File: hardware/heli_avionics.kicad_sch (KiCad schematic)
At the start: 15 parts, among them J1 Pin_Header_2x3, J7 JST_ZH_01x02, SW1 Reset, U1 ATmega4808-A

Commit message: Added mounting holes and did board outline
Also tried an initial layout with some components
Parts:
- added H1, H2, H3: MountingHole, MountingHole:MountingHole_2mm, symbol Mechanical:MountingHole
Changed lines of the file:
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@@
+		)
+	)
+	(rectangle
+		(start 243.84 124.46)
+		(end 271.78 152.4)
+		(stroke
+			(width 0)
+			(type dash_dot_dot)
+		)
+		(fill
+			(type none)
 		)
 	)
@@
 	)
 	(symbol
+		(lib_id "Mechanical:MountingHole")
+		(at 250.19 146.05 0)
+		(unit 1)
+		(exclude_from_sim yes)
+		(in_bom no)
+		(on_board yes)
+		(dnp no)
+		(fields_autoplaced yes)
+		(property "Reference" "H3"
+			(at 252.73 144.7799 0)
+			(effects
+				(font
+					(size 1.27 1.27)
+				)
+				(justify left)
+			)
+		)
+		(property "Value" "MountingHole"
+			(at 252.73 147.3199 0)
+			(effects
+				(font
+					(size 1.27 1.27)
+				)
+				(justify left)
+			)
+		)
+		(property "Footprint" "MountingHole:MountingHole_2mm"
+			(at 250.19 146.05 0)
+			(effects
+				(font
+					(size 1.27 1.27)
+				)
+				(hide yes)
+			)
+		)
+		(property "Datasheet" "~"
+			(at 250.19 146.05 0)
+			(effects
+				(font
+					(size 1.27 1.27)
+				)
+				(hide yes)
+			)
+		)
+		(property "Description" "Mounting Hole without connection"
+			(at 250.19 146.05 0)
+			(effects
+				(font
+					(size 1.27 1.27)
+				)
+				(hide yes)
+			)
+		)
+		(instances
+			(project ""
+				(path "/c384ea46-0dfb-4673-b2f4-1f88fafbcaa5"
+					(reference "H3")
+					(unit 1)
+				)
+			)
+		)
+	)
+	(symbol
 		(lib_id "Device:C")
 		(at 60.96 68.58 0)
@@
 	)
 	(symbol
+		(lib_id "Mechanical:MountingHole")
+		(at 250.19 138.43 0)
+		(unit 1)
+		(exclude_from_sim yes)
+		(in_bom no)
+		(on_board yes)
+		(dnp no)
+		(fields_autoplaced yes)
+		(property "Reference" "H2"
+			(at 252.73 137.1599 0)
+			(effects
+				(font
+					(size 1.27 1.27)
+				)
+				(justify left)
+			)
+		)
+		(property "Value" "MountingHole"
+			(at 252.73 139.6999 0)
+			(effects
+				(font
+					(size 1.27 1.27)
+				)
+				(justify left)
+			)
+		)
+		(property "Footprint" "MountingHole:MountingHole_2mm"
+			(at 250.19 138.43 0)
+			(effects
+				(font
+					(size 1.27 1.27)
+				)
+				(hide yes)
+			)
+		)
+		(property "Datasheet" "~"
+			(at 250.19 138.43 0)
+			(effects
+				(font
+					(size 1.27 1.27)
+				)
+				(hide yes)
+			)
+		)
+		(property "Description" "Mounting Hole without connection"
+			(at 250.19 138.43 0)
+			(effects
+				(font
+					(size 1.27 1.27)
+				)
+				(hide yes)
+			)
+		)
+		(instances
+			(project ""
+				(path "/c384ea46-0dfb-4673-b2f4-1f88fafbcaa5"
+					(reference "H2")
+					(unit 1)
+				)
+			)
+		)
+	)
+	(symbol
 		(lib_id "power:GND")
 		(at 205.74 106.68 0)
@@
 					(unit 1)
 				)
+			)
+		)
+	)
+	(symbol
+		(lib_id "Mechanical:MountingHole")
+		(at 250.19 130.81 0)
+		(unit 1)
+		(exclude_from_sim yes)
+		(in_bom no)
+		(on_board yes)
+		(dnp no)
+		(fields_autoplaced yes)
+		(property "Reference" "H1"
+			(at 252.73 129.5399 0)
+			(effects
+				(font
+					(size 1.27 1.27)
+				)
+				(justify left)
+			)
+		)
+		(property "Value" "MountingHole"
+			(at 252.73 132.0799 0)
+			(effects
+				(font
+					(size 1.27 1.27)
+				)
+				(justify left)
+			)
+		)
+		(property "Footprint" "MountingHole:MountingHole_2mm"
+			(at 250.19 130.81 0)
+			(effects
+				(font
+					(size 1.27 1.27)
+				)
+				(hide yes)
+			)
+		)
+		(property "Datasheet" "~"
+			(at 250.19 130.81 0)
+			(effects
+				(font
+					(size 1.27 1.27)
+				)
+				(hide yes)
+			)
+		)
+		(property "Description" "Mounting Hole without connection"
+			(at 250.19 130.81 0)
+			(effects
+				(font
+					(size 1.27 1.27)
+				)
+				(hide yes)
+			)
+		)
+		(instances
+			(project ""
+				(path "/c384ea46-0dfb-4673-b2f4-1f88fafbcaa5"
+					(reference "H1")
+					(unit 1)
+				)

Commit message: Assigned footprints for capacitors and inductors
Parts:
- C1, C2, C28, C29, C3: footprint (none) -> Capacitor_SMD:C_0603_1608Metric_Pad1.08x0.95mm_HandSolder
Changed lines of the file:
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@@
 			)
 		)
-		(property "Footprint" ""
+		(property "Footprint" "Capacitor_SMD:C_0603_1608Metric_Pad1.08x0.95mm_HandSolder"
 			(at 241.6048 39.37 0)
 			(effects
@@
 			)
 		)
-		(property "Footprint" ""
+		(property "Footprint" "Capacitor_SMD:C_0603_1608Metric_Pad1.08x0.95mm_HandSolder"
 			(at 61.9252 72.39 0)
 			(effects
@@
 			)
 		)
-		(property "Footprint" ""
+		(property "Footprint" "Capacitor_SMD:C_0603_1608Metric_Pad1.08x0.95mm_HandSolder"
 			(at 228.2952 39.37 0)
 			(effects
@@
 			)
 		)
-		(property "Footprint" ""
+		(property "Footprint" "Capacitor_SMD:C_0603_1608Metric_Pad1.08x0.95mm_HandSolder"
 			(at 121.92 51.1048 0)
 			(effects
@@
 			)
 		)
-		(property "Footprint" ""
+		(property "Footprint" "Capacitor_SMD:C_0603_1608Metric_Pad1.08x0.95mm_HandSolder"
 			(at 255.5748 39.37 0)
 			(effects

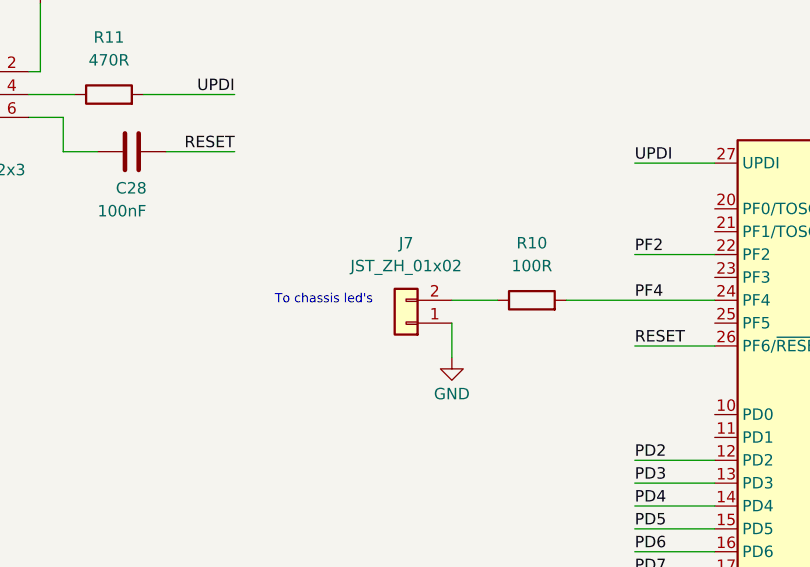
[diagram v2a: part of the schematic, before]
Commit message: Corrected pin order on JST connectors
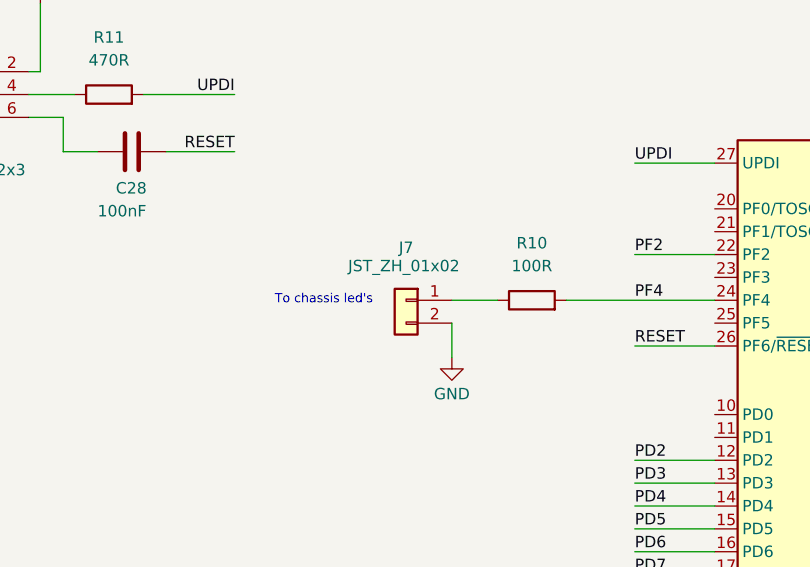
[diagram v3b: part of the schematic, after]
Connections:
- net GND: now also J7.2 (Pin_2); no longer J7.1 (Pin_1)
- net at R10.1: now also J7.1 (Pin_1); no longer J7.2 (Pin_2)
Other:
- moved on the sheet: J7
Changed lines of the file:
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@@
+	(wire
+		(pts
+			(xy 161.29 71.12) (xy 161.29 74.93)
+		)
+		(stroke
+			(width 0)
+			(type default)
+		)
+	)
 	(wire
 		(pts
@@
 		(pts
 			(xy 220.98 60.96) (xy 232.41 60.96)
-		)
-		(stroke
-			(width 0)
-			(type default)
-		)
-	)
-	(wire
-		(pts
-			(xy 161.29 71.12) (xy 161.29 74.93)
 		)
 		(stroke
@@
 	(symbol
 		(lib_id "Connector_Generic:Conn_01x02")
-		(at 156.21 71.12 180)
+		(at 156.21 68.58 0)
+		(mirror y)
 		(unit 1)
 		(exclude_from_sim no)
@@
 		(on_board yes)
 		(dnp no)
-		(fields_autoplaced yes)
 		(property "Reference" "J7"
-			(at 156.21 62.23 0)
+			(at 156.21 62.738 0)
 			(effects
 				(font
@@
 		)
 		(property "Value" "JST_ZH_01x02"
-			(at 156.21 64.77 0)
+			(at 155.956 64.77 0)
 			(effects
 				(font
@@
 		)
 		(property "Footprint" "Connector_JST:JST_ZH_B2B-ZR_1x02_P1.50mm_Vertical"
-			(at 156.21 71.12 0)
+			(at 156.21 68.58 0)
 			(effects
 				(font
@@
 		)
 		(property "Datasheet" "~"
-			(at 156.21 71.12 0)
+			(at 156.21 68.58 0)
 			(effects
 				(font
@@
 		)
 		(property "Description" "Generic connector, single row, 01x02, script generated (kicad-library-utils/schlib/autogen/connector/)"
-			(at 156.21 71.12 0)
+			(at 156.21 68.58 0)
 			(effects
 				(font

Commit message: Assigned resistor footprints
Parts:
- R1, R10, R11, R2, R9: footprint (none) -> Resistor_SMD:R_0603_1608Metric_Pad0.98x0.95mm_HandSolder
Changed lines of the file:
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@@
 			)
 		)
-		(property "Footprint" ""
+		(property "Footprint" "Resistor_SMD:R_0603_1608Metric_Pad0.98x0.95mm_HandSolder"
 			(at 46.99 66.548 90)
 			(effects
@@
 			)
 		)
-		(property "Footprint" ""
+		(property "Footprint" "Resistor_SMD:R_0603_1608Metric_Pad0.98x0.95mm_HandSolder"
 			(at 62.738 58.42 90)
 			(effects
@@
 			)
 		)
-		(property "Footprint" ""
+		(property "Footprint" "Resistor_SMD:R_0603_1608Metric_Pad0.98x0.95mm_HandSolder"
 			(at 170.18 70.358 90)
 			(effects
@@
 			)
 		)
-		(property "Footprint" ""
+		(property "Footprint" "Resistor_SMD:R_0603_1608Metric_Pad0.98x0.95mm_HandSolder"
 			(at 241.3 77.978 90)
 			(effects
@@
 			)
 		)
-		(property "Footprint" ""
+		(property "Footprint" "Resistor_SMD:R_0603_1608Metric_Pad0.98x0.95mm_HandSolder"
 			(at 123.19 47.498 90)
 			(effects

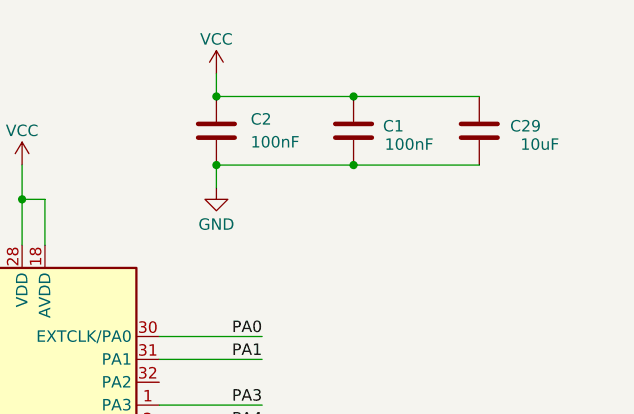
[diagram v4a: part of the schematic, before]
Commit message: Updated decoupling caps to match guidelines from Eric Bogatin
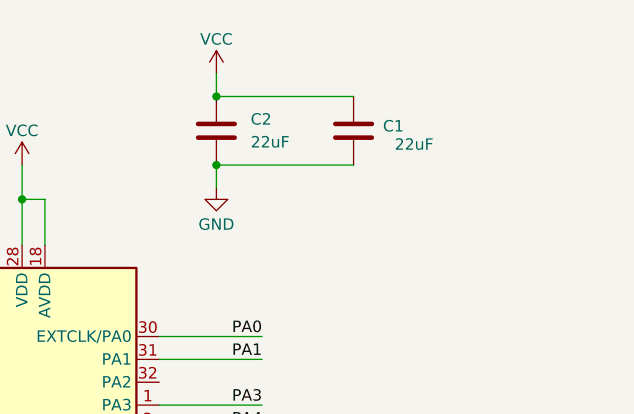
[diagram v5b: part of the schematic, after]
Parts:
- removed C29: 10uF, Capacitor_SMD:C_0603_1608Metric_Pad1.08x0.95mm_HandSolder, symbol Device:C
- C1, C2: value 100nF -> 22uF
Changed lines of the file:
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@@
 	(paper "A4")
-	(junction
-		(at 242.57 31.75)
-		(diameter 0)
-		(color 0 0 0 0)
-	)
-	(junction
-		(at 242.57 39.37)
-		(diameter 0)
-		(color 0 0 0 0)
-	)
 	(junction
 		(at 205.74 43.18)
@@
 	(wire
 		(pts
-			(xy 242.57 31.75) (xy 256.54 31.75)
-		)
-		(stroke
-			(width 0)
-			(type default)
-		)
-	)
-	(wire
-		(pts
 			(xy 67.31 143.51) (xy 77.47 143.51)
 		)
@@
 		(pts
 			(xy 165.1 140.97) (xy 173.99 140.97)
-		)
-		(stroke
-			(width 0)
-			(type default)
-		)
-	)
-	(wire
-		(pts
-			(xy 242.57 39.37) (xy 256.54 39.37)
 		)
 		(stroke
@@
 			)
 		)
-		(property "Value" "100nF"
+		(property "Value" "22uF"
 			(at 251.46 37.084 0)
 			(effects
@@
 			)
 		)
-		(property "Value" "100nF"
+		(property "Value" "22uF"
 			(at 231.14 36.8299 0)
 			(effects
@@
 					(unit 1)
 				)
-			)
-		)
-	)
-	(symbol
-		(lib_id "Device:C")
-		(at 256.54 35.56 0)
-		(mirror y)
-		(unit 1)
-		(exclude_from_sim no)
-		(in_bom yes)
-		(on_board yes)
-		(dnp no)
-		(property "Reference" "C29"
-			(at 263.398 35.052 0)
-			(effects
-				(font
-					(size 1.27 1.27)
-				)
-				(justify left)
-			)
-		)
-		(property "Value" "10uF"
-			(at 265.43 37.084 0)
-			(effects
-				(font
-					(size 1.27 1.27)
-				)
-				(justify left)
-			)
-		)
-		(property "Footprint" "Capacitor_SMD:C_0603_1608Metric_Pad1.08x0.95mm_HandSolder"
-			(at 255.5748 39.37 0)
-			(effects
-				(font
-					(size 1.27 1.27)
-				)
-				(hide yes)
-			)
-		)
-		(property "Datasheet" "~"
-			(at 256.54 35.56 0)
-			(effects
-				(font
-					(size 1.27 1.27)
-				)
-				(hide yes)
-			)
-		)
-		(property "Description" "Unpolarized capacitor"
-			(at 256.54 35.56 0)
-			(effects
-				(font
-					(size 1.27 1.27)
-				)
-				(hide yes)
-			)
-		)
-		(pin "2"
-		)
-		(pin "1"
-		)
-		(instances
-			(project "heli_avionics"
-				(path "/c384ea46-0dfb-4673-b2f4-1f88fafbcaa5"
-					(reference "C29")
-					(unit 1)
-				)
